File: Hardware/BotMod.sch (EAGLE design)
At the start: 42 parts, among them Q1 BSS138, Q2 BSS138, T1 MMBT2222A, U1 LSM303D

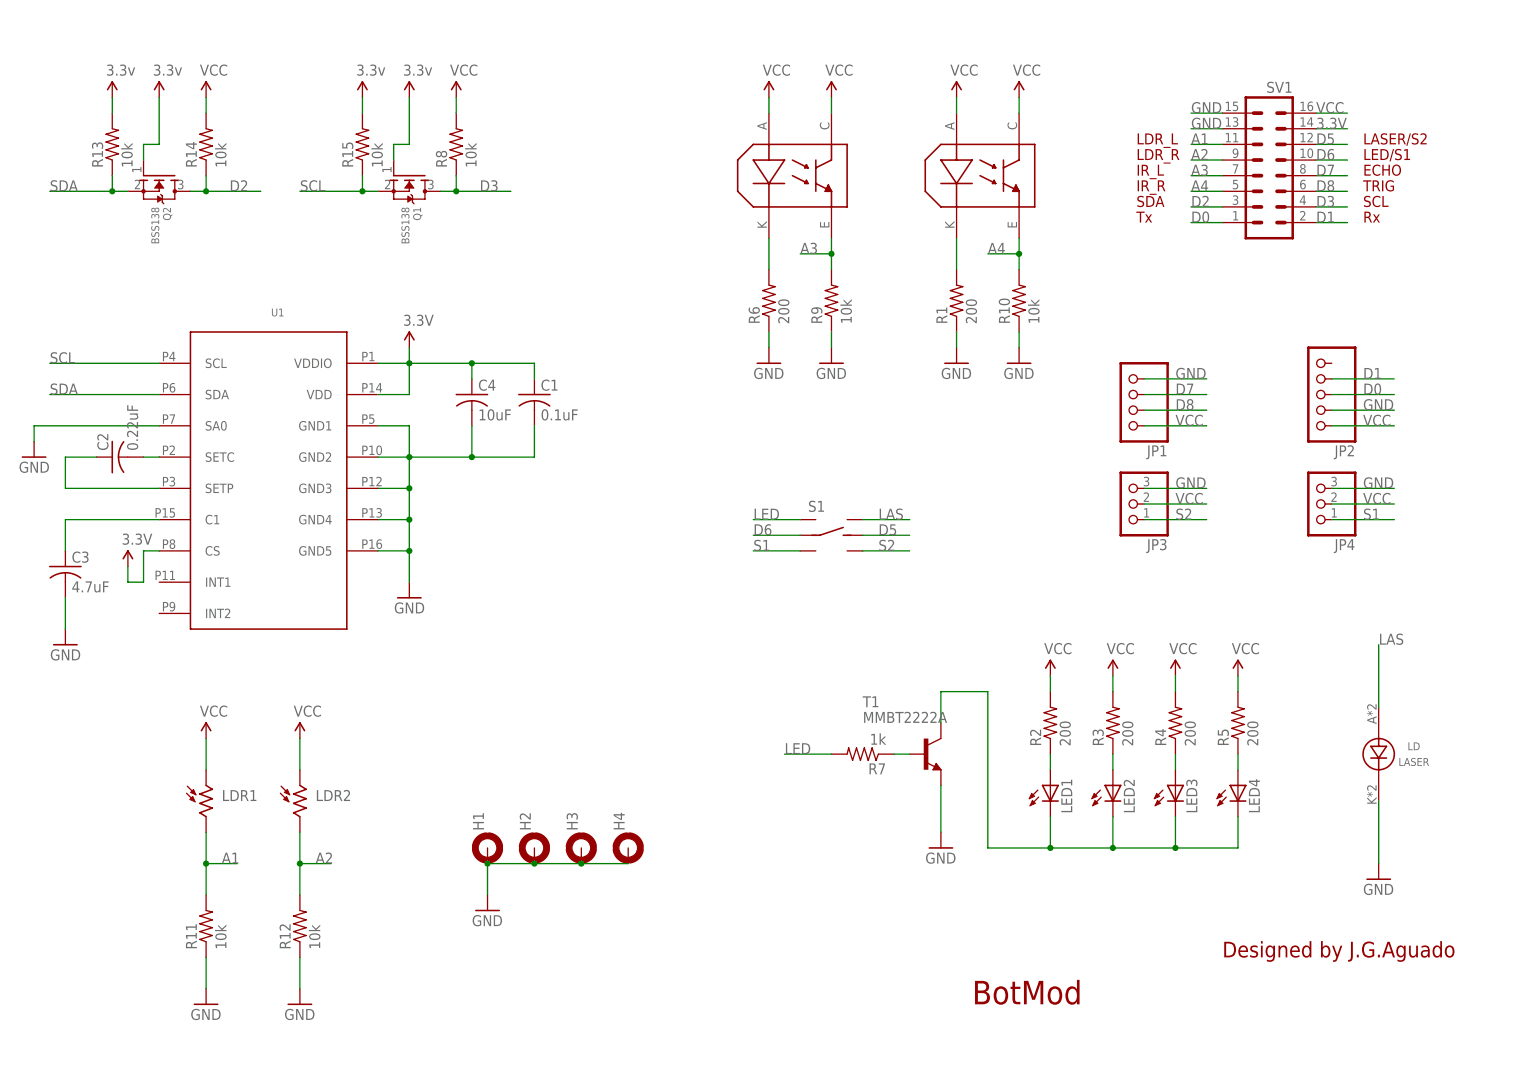
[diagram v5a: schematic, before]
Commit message: Redesigned BotMod (R2) with support for:  - ToF distance sensors VL6180X (5-100mm) and VL53L1X (40-4000mm)  - SMD High Intensity Led
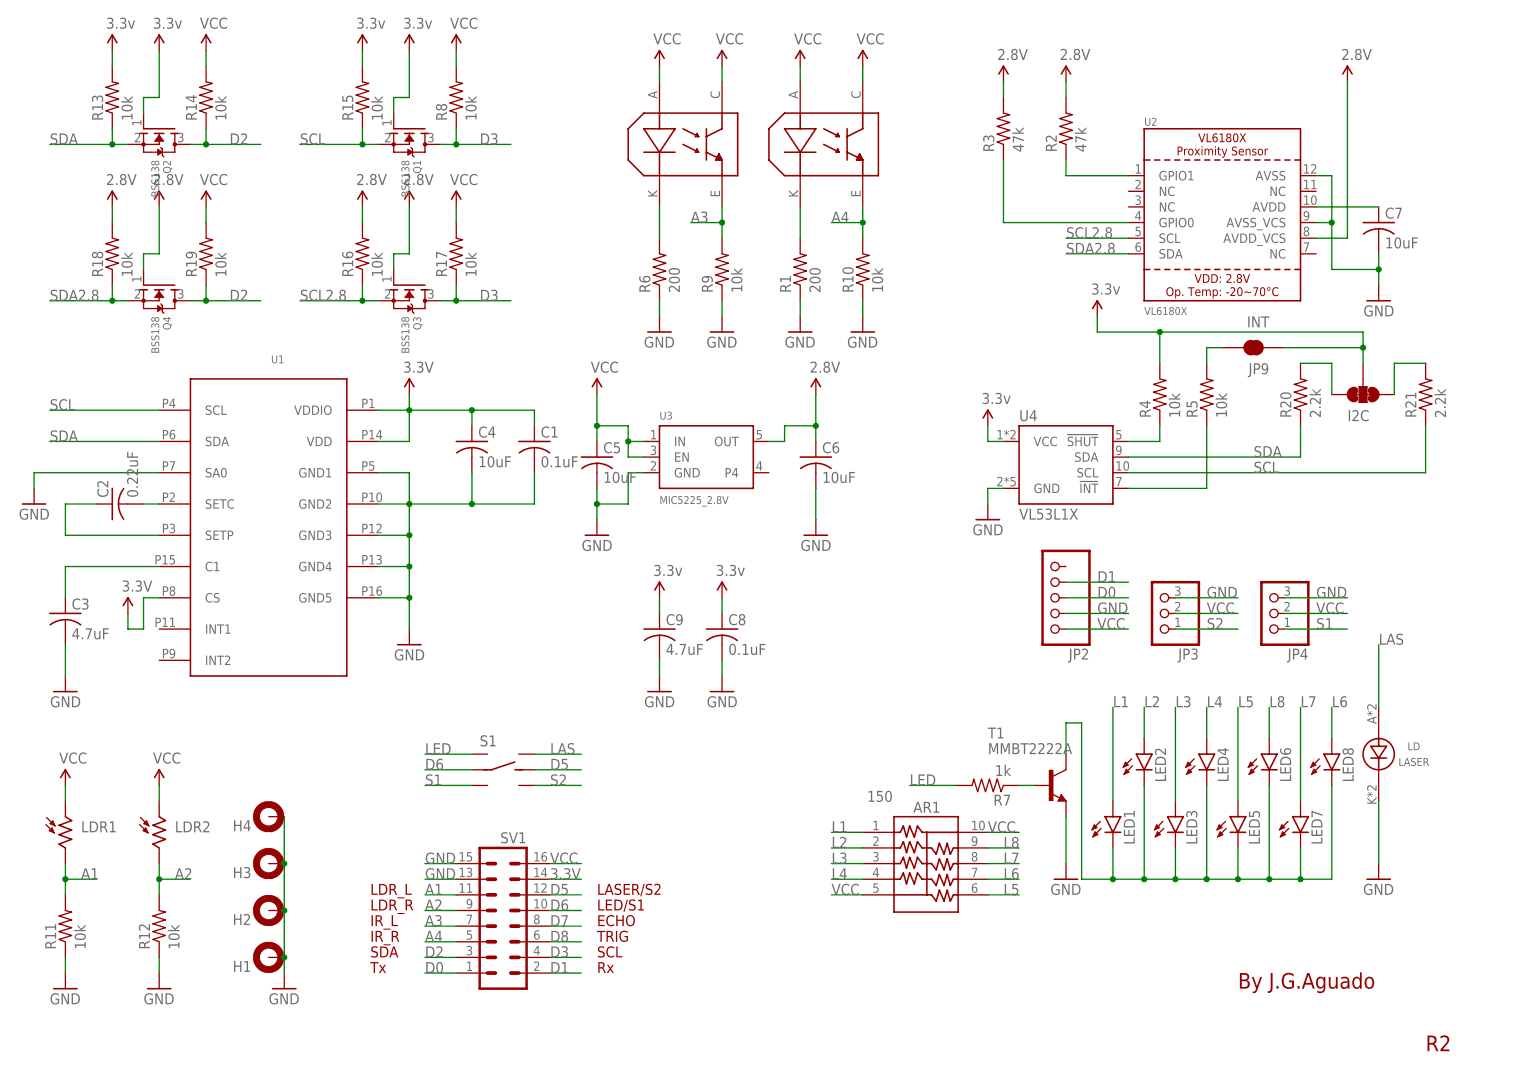
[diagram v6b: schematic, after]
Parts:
- removed JP1: PINHEAD_4_FEMALE, SpaceDIY_connectors:PINHEAD_4_FEMALE
- added AR1: 150, SpaceDIY:RESISTOR_ARRAY_X8_CAY17
- added C5, C6, C7: 10uF, Passive_components:C0402
- added C8: 0.1uF, Passive_components:C0402
- added C9: 4.7uF, Passive_components:C0402
- added I2C: JUMPER-SMT_3_2-NC_TRACE_SILK, SparkFun-Jumpers:JUMPER-SMT_3_2-NC_TRACE_SILK
- added JP9: INT, SparkFun-Passives:JUMPER-PAD-2-NC_BY_TRACE
- added LED5, LED6, LED7, LED8: (no value), led:LEDSML1206
- added Q3, Q4: BSS138, adafruit:MOSFET-NREFLOW
- added R16, R17, R18, R19: 10k, Passive_components:R0402
- added R20, R21: 2.2k, Passive_components:R0402
- added U2: VL6180X, microbuilder:VL6180X
- added U3: MIC5225_2.8V, microbuilder:VREG_SOT23-5
- added U4: VL53L1X, SparkFun-Sensors:VL53L1XSMD
- C1, C2, C3, C4: device resistor:C-USC1206 -> Passive_components:C0402
- LED1, LED2, LED3, LED4: device led:LED5MM -> led:LEDSML1206
- R1, R10, R11, R12, R13, R14, R15, R6, R7, R8, R9: device resistor:R-US_R1206 -> Passive_components:R0402
- R2, R3: value 200 -> 47k; device resistor:R-US_R1206 -> Passive_components:R0402
- R4, R5: value 200 -> 10k; device resistor:R-US_R1206 -> Passive_components:R0402
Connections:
- new net 2.8V: C6.1, Q3.G, Q4.G, R16.2, R18.2, R2.2, R3.2, U2.AVDD_VCS, U3.OUT
- new net L1: AR1.1, LED1.A
- new net L2: AR1.2, LED2.A
- new net L3: AR1.3, LED3.A
- new net L4: AR1.4, LED4.A
- new net L5: AR1.6, LED5.A
- new net L6: AR1.7, LED8.A
- new net L7: AR1.8, LED7.A
- new net L8: AR1.9, LED6.A
- new net N$14: JP9.2, R5.2
- new net N$16: R4.1, U4.!SHUT
- new net N$19: R5.1, U4.!INT
- new net N$9: I2C.1, R21.2
- new net SCL2.8: Q3.S, R16.1, U2.SCL
- new net SDA2.8: Q4.S, R18.1, U2.SDA
- net 3.3V: now also C8.1, C9.1, I2C.2, JP9.1, R4.2, U4.VCC
- net D2: now also Q4.D, R19.1
- net D3: now also Q3.D, R17.1
- net D7: no longer JP1.3
- net D8: no longer JP1.2
- net GND: now also C5.2, C6.2, C7.2, C8.2, C9.2, U2.AVSS, U2.AVSS_VCS, U3.GND, U4.GND; no longer JP1.4
- net N$1: now also LED5.C, LED6.C, LED7.C, LED8.C
- net N$5: now also U2.GPIO1; no longer LED1.A
- net N$6: now also U2.GPIO0; no longer LED2.A
- net N$7: now also I2C.3, R20.2; no longer LED3.A, R4.1
- net N$8: now also C7.1, U2.AVDD; no longer LED4.A, R5.1
- net SCL: now also R21.1, U4.SCL
- net SDA: now also R20.1, U4.SDA
- net VCC: now also AR1.10, AR1.5, C5.1, R17.2, R19.2, U3.EN, U3.IN; no longer JP1.1, R2.2, R3.2, R4.2, R5.2
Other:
- note added: "By J.G.Aguado"
- note added: "R2"
- note removed: "BotMod"
- note removed: "Designed by J.G.Aguado"
- moved on the sheet: C1, C2, C3, C4, H1, H2, H3, H4, JP2, JP3, JP4, LDR1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

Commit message: Updated LED Resistors
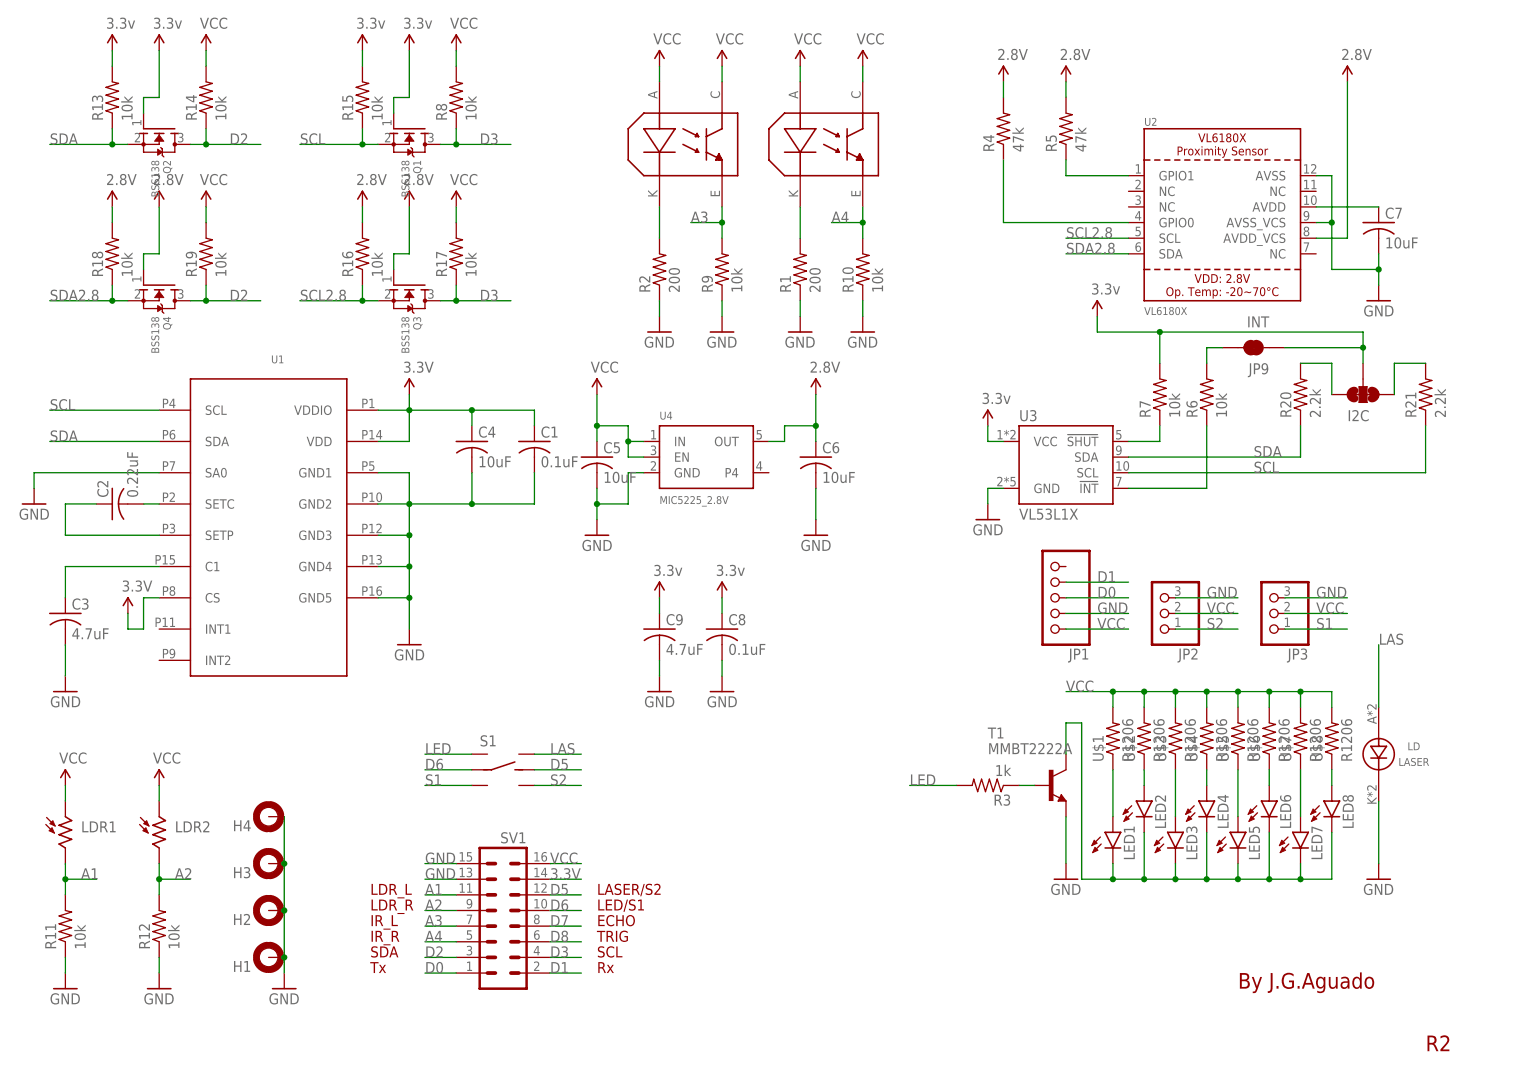
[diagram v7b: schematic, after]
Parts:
- removed AR1: 150, SpaceDIY:RESISTOR_ARRAY_X8_CAY17
- removed JP4: (no value), pinhead:PINHD-1X3
- added JP1: PINHEAD_5_FEMALE, SpaceDIY_connectors:PINHEAD_5_FEMALE
- added U$1, U$2, U$3, U$4, U$5, U$6, U$7, U$8: R1206, Passive_components:R1206
- JP2: value PINHEAD_5_FEMALE -> (none); device SpaceDIY_connectors:PINHEAD_5_FEMALE -> pinhead:PINHD-1X3
- R2: value 47k -> 200
- R3: value 47k -> 1k
- R4, R5: value 10k -> 47k
- R6: value 200 -> 10k
- R7: value 1k -> 10k
- U3: value MIC5225_2.8V -> VL53L1X; device microbuilder:VREG_SOT23-5 -> SparkFun-Sensors:VL53L1XSMD
- U4: value VL53L1X -> MIC5225_2.8V; device SparkFun-Sensors:VL53L1XSMD -> microbuilder:VREG_SOT23-5
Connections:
- net 2.8V: now also R4.2, R5.2, U4.OUT; no longer R2.2, R3.2, U3.OUT
- net 3.3V: now also R7.2, U3.VCC; no longer R4.2, U4.VCC
- net D0: now also JP1.3; no longer JP2.3
- net D1: now also JP1.4; no longer JP2.4
- net GND: now also JP1.2, JP2.3, R2.1; no longer JP2.2, JP4.3, R6.1
- net L1: now also U$1.1; no longer AR1.1
- net L2: now also U$2.1; no longer AR1.2
- net L3: now also U$3.1; no longer AR1.3
- net L4: now also U$4.1; no longer AR1.4
- net L5: now also U$5.1; no longer AR1.6
- net L6: now also U$8.1; no longer AR1.7
- net L7: now also U$7.1; no longer AR1.8
- net L8: now also U$6.1; no longer AR1.9
- net LED: now also R3.2; no longer R7.2
- net N$14: now also R6.2; no longer R5.2
- net N$16: now also R7.1, U3.!SHUT; no longer R4.1, U4.!SHUT
- net N$19: now also R6.1, U3.!INT; no longer R5.1, U4.!INT
- net N$2: now also R3.1; no longer R7.1
- net N$3: now also R2.2; no longer R6.2
- net N$5: now also R5.1; no longer R2.1
- net N$6: now also R4.1; no longer R3.1
- net S1: now also JP3.1; no longer JP4.1
- net S2: now also JP2.1; no longer JP3.1
- net SCL: now also U3.SCL; no longer U4.SCL
- net SDA: now also U3.SDA; no longer U4.SDA
- net VCC: now also JP1.1, JP2.2, U$1.2, U$2.2, U$3.2, U$4.2, U$5.2, U$6.2, U$7.2, U$8.2, U4.EN, U4.IN; no longer AR1.10, AR1.5, JP2.1, JP4.2, U3.EN, U3.IN
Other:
- moved on the sheet: JP3, LED1, LED2, LED3, LED4, LED5, LED6, LED7, LED8, R2, R3, R4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

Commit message: Replaced LED lights with 7310 package
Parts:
- removed U$1, U$3, U$5, U$7: R1206, Passive_components:R1206
- added R22, R24, R26, R28: R1206, Passive_components:R1206
- LED1, LED2, LED3, LED4, LED5, LED6, LED7, LED8: value (none) -> LED5730; device led:LEDSML1206 -> SpaceDIY_passive_components:LED5730
- renumbered U$2 to R23, U$4 to R25, U$6 to R27, U$8 to R29
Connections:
- net L1: now also R22.1; no longer U$1.1
- net L3: now also R24.1; no longer U$3.1
- net L5: now also R26.1; no longer U$5.1
- net L7: now also R28.1; no longer U$7.1
- net VCC: now also R22.2, R24.2, R26.2, R28.2; no longer U$1.2, U$3.2, U$5.2, U$7.2
